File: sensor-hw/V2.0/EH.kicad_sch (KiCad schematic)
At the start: 41 parts, among them J1 Conn_01x03_Male, J10 Conn_01x03_Male, J11 Conn_01x04_Male, J12 Conn_01x03_Male, J13 Conn_01x03_Male, J14 Conn_01x03_Male, J15 Screw_Terminal_01x02, J19 Conn_01x03_Male, J2 Conn_01x03_Male, J25 Conn_01x02_Male, J3 Conn_01x03_Male, J4 Conn_01x03_Male, J5 Conn_01x03_Male, J6 Conn_01x03_Male, J7 Conn_01x03_Male, J8 Conn_01x03_Male, J9 Conn_01x03_Male, U1 LTC3331

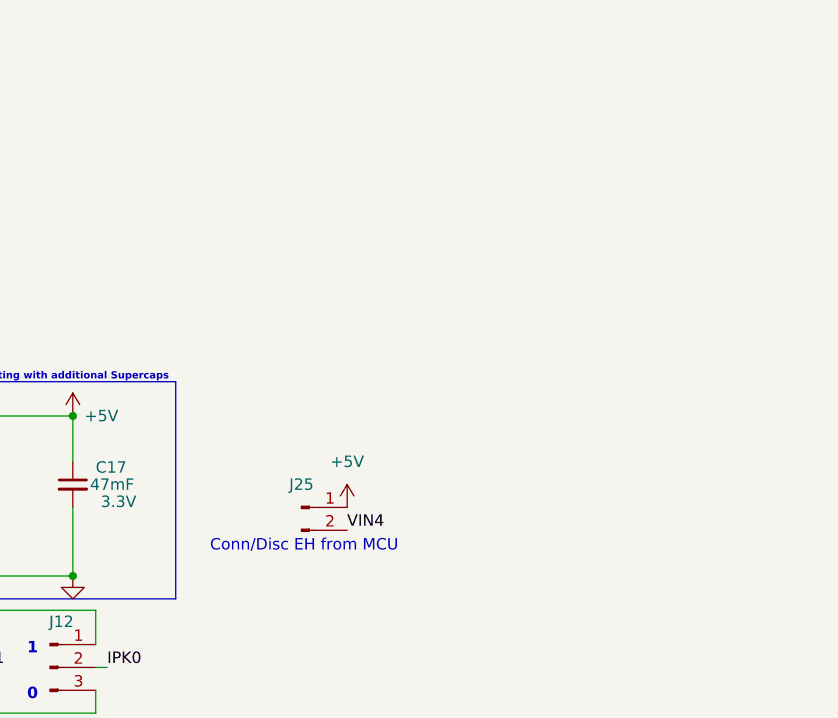
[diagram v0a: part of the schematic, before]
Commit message: Added the Power section.
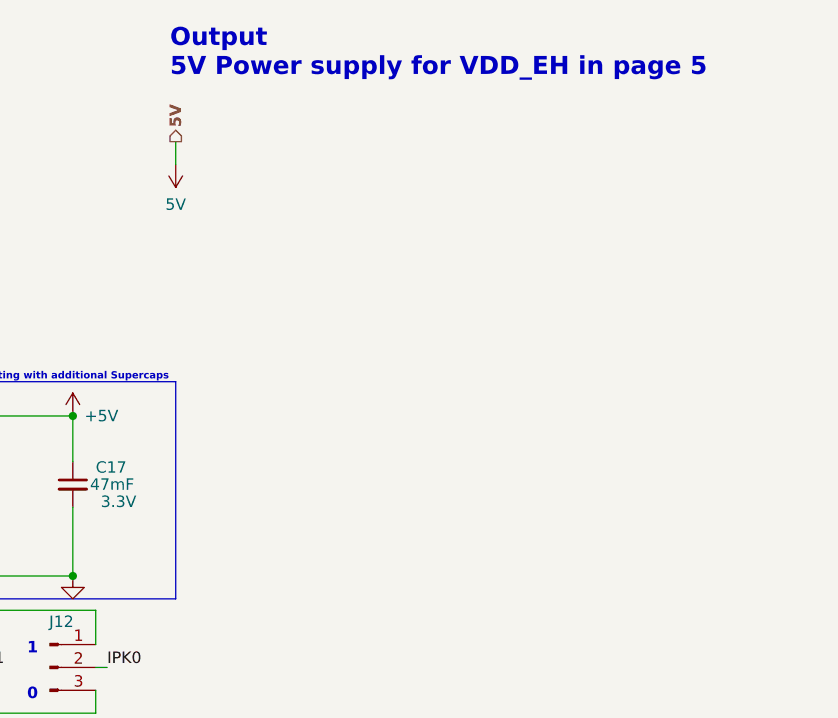
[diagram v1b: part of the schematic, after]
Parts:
- removed J25: Conn_01x02_Male, Connector_PinSocket_2.54mm:PinSocket_1x02_P2.54mm_Vertical, symbol Connector:Conn_01x02_Male
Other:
- note added: "Output 5V Power supply for VDD_EH in page 5"
- note removed: "Conn/Disc EH from MCU"
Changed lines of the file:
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@@
+    (stroke (width 0) (type default))
+  )
+  (wire (pts (xy 220.345 28.575) (xy 220.345 31.115))
     (stroke (width 0) (type default))
   )
@@
   (text "0\n" (at 106.045 140.335 0)
     (effects (font (size 1.27 1.27) bold) (justify left bottom))
+  )
+  (text "Output\n5V Power supply for VDD_EH in page 5\n\n" (at 219.71 24.765 0)
+    (effects (font (size 2 2) bold) (justify left bottom) (href "#2"))
   )
   (text "0\n" (at 201.295 111.125 0)
@@
     (effects (font (size 1.27 1.27) bold) (justify left bottom))
   )
-  (text "Conn/Disc EH from MCU" (at 224.155 74.295 0)
-    (effects (font (size 1.27 1.27)) (justify left bottom))
-  )
   (text "IPK0\n\n\n" (at 204.47 99.695 0)
     (effects (font (size 1.27 1.27)) (justify left bottom))
@@
     (effects (font (size 1.27 1.27)) (justify left bottom))
   )
-  (label "VIN4" (at 239.395 71.755 0) (fields_autoplaced)
-    (effects (font (size 1.27 1.27)) (justify left bottom))
-  )
   (label "OUT2" (at 178.435 107.315 0) (fields_autoplaced)
     (effects (font (size 1.27 1.27)) (justify left bottom))
@@
   (label "OUT2" (at 153.035 99.695 0) (fields_autoplaced)
     (effects (font (size 1.27 1.27)) (justify left bottom))
+  )
+  (hierarchical_label "5V" (shape output) (at 220.345 28.575 90) (fields_autoplaced)
+    (effects (font (size 1.27 1.27) bold) (justify left))
   )
   (symbol (lib_id "Device:L_Small") (at 158.115 52.705 90) (unit 1)
@@
         (path "/55528413-c8da-463c-8fa0-4d866d881d6a/2cbc6153-932e-440a-8371-60dc02b8f5df"
           (reference "J13") (unit 1)
-        )
-      )
-    )
-  )
-  (symbol (lib_id "Connector:Conn_01x02_Male") (at 234.315 69.215 0) (unit 1)
-    (in_bom yes) (on_board yes) (dnp no)
-    (property "Reference" "J25" (at 234.315 66.675 0)
-      (effects (font (size 1.27 1.27)))
-    )
-    (property "Value" "Conn_01x02_Male" (at 234.95 66.675 0)
-      (effects (font (size 1.27 1.27)) hide)
-    )
-    (property "Footprint" "Connector_PinSocket_2.54mm:PinSocket_1x02_P2.54mm_Vertical" (at 234.315 69.215 0)
-      (effects (font (size 1.27 1.27)) hide)
-    )
-    (property "Datasheet" "~" (at 234.315 69.215 0)
-      (effects (font (size 1.27 1.27)) hide)
-    )
-    (pin "1")
-    (pin "2")
-    (instances
-      (project "beta_prototype"
-        (path "/39c3f2e4-c15d-4dcf-8488-7b897a1552e9"
-          (reference "J25") (unit 1)
-        )
-        (path "/39c3f2e4-c15d-4dcf-8488-7b897a1552e9/1cdc1c17-3bc9-475f-90f2-f21656679460"
-          (reference "J2") (unit 1)
-        )
-      )
-      (project "sensor-hw"
-        (path "/55528413-c8da-463c-8fa0-4d866d881d6a/2cbc6153-932e-440a-8371-60dc02b8f5df"
-          (reference "J25") (unit 1)
         )
       )
@@
     )
   )
+  (symbol (lib_id "Local:5V") (at 220.345 31.115 180) (unit 1)
+    (in_bom yes) (on_board yes) (dnp no) (fields_autoplaced)
+    (property "Reference" "#PWR015" (at 220.345 27.305 0)
+      (effects (font (size 1.27 1.27)) hide)
+    )
+    (property "Value" "5V" (at 220.345 35.56 0)
+      (effects (font (size 1.27 1.27)))
+    )
+    (property "Footprint" "" (at 220.345 31.115 0)
+      (effects (font (size 1.27 1.27)) hide)
+    )
+    (property "Datasheet" "" (at 220.345 31.115 0)
+      (effects (font (size 1.27 1.27)) hide)
+    )
+    (pin "1")
+    (instances
+      (project "sensor-hw"
+        (path "/55528413-c8da-463c-8fa0-4d866d881d6a/2cbc6153-932e-440a-8371-60dc02b8f5df"
+          (reference "#PWR015") (unit 1)
+        )
+      )
+    )
+  )
   (symbol (lib_id "power:PWR_FLAG") (at 145.415 118.745 270) (unit 1)
     (in_bom yes) (on_board yes) (dnp no) (fields_autoplaced)
@@
         )
       )
-    )
-  )
-  (symbol (lib_id "power:+5V") (at 239.395 69.215 0) (unit 1)
-    (in_bom yes) (on_board yes) (dnp no)
-    (property "Reference" "#PWR0114" (at 239.395 73.025 0)
-      (effects (font (size 1.27 1.27)) hide)
-    )
-    (property "Value" "+5V" (at 239.395 64.135 0)
-      (effects (font (size 1.27 1.27)))
-    )
-    (property "Footprint" "" (at 239.395 69.215 0)
-      (effects (font (size 1.27 1.27)) hide)
-    )
-    (property "Datasheet" "" (at 239.395 69.215 0)
-      (effects (font (size 1.27 1.27)) hide)
-    )
-    (pin "1")
-    (instances
-      (project "beta_prototype"
-        (path "/39c3f2e4-c15d-4dcf-8488-7b897a1552e9"
-          (reference "#PWR0114") (unit 1)
-        )
-        (path "/39c3f2e4-c15d-4dcf-8488-7b897a1552e9/1cdc1c17-3bc9-475f-90f2-f21656679460"
-          (reference "#PWR06") (unit 1)
-        )
-      )
-      (project "sensor-hw"
-        (path "/55528413-c8da-463c-8fa0-4d866d881d6a/2cbc6153-932e-440a-8371-60dc02b8f5df"
-          (reference "#PWR0114") (unit 1)
-        )
-      )
